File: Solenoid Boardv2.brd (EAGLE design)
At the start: 76.2 x 31.8 mm, 52 parts, among them Y2 ECS-80-S-4X

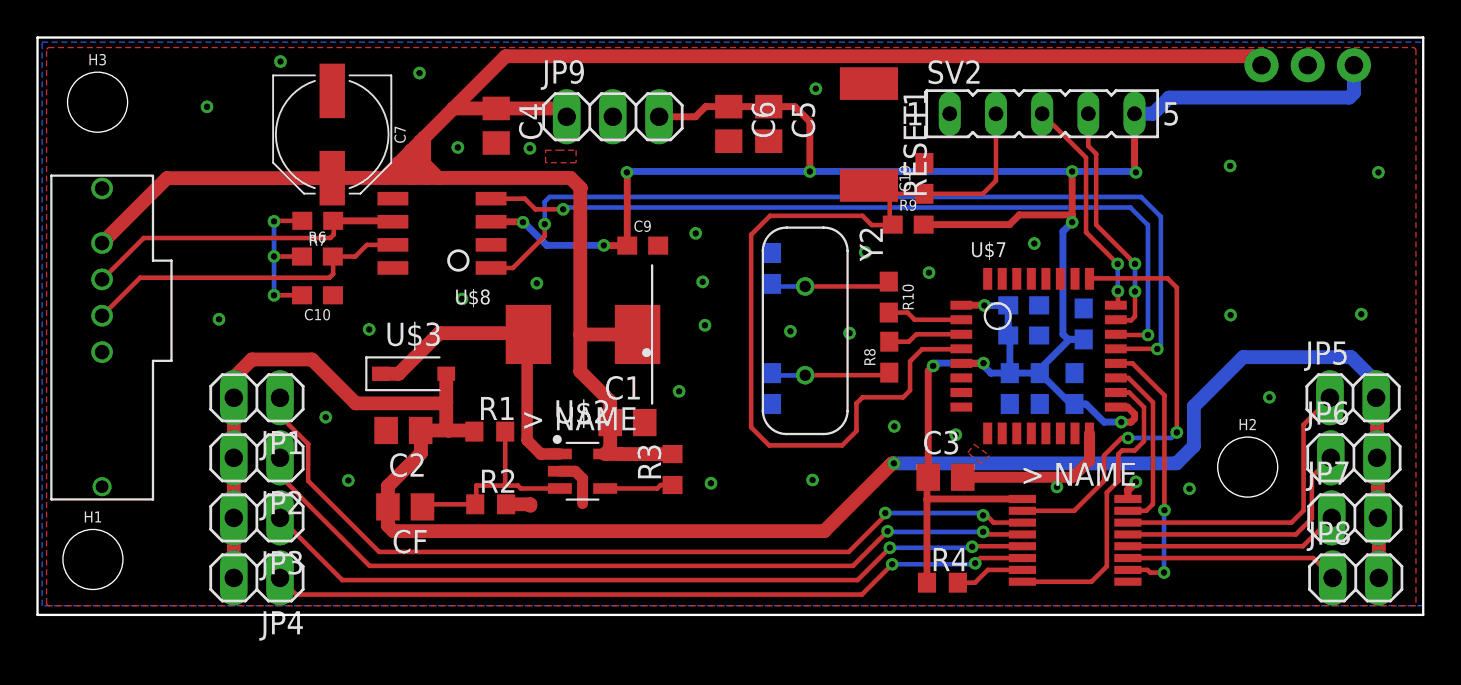
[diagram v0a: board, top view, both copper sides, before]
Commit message: fixed a weird trace, moved a standoff hole a little so that it didnt overlap with a trace
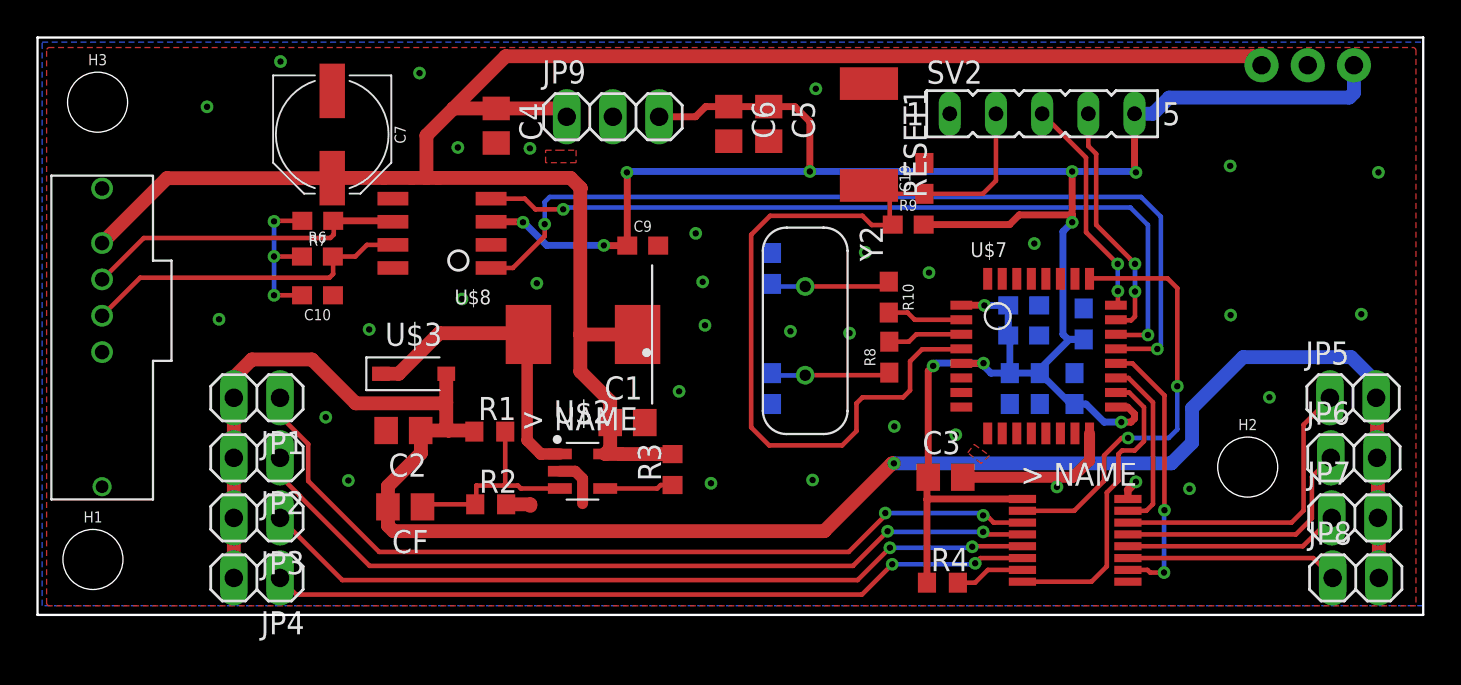
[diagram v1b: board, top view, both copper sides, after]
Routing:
- net +12V: track 115.5 -> 107.0 mm
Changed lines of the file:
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@@
 <wire x1="28.642" y1="27.85" x2="25.224" y2="27.85" width="0.762" layer="1"/>
 <wire x1="25.224" y1="27.85" x2="22.8716" y2="27.85" width="0.762" layer="1"/>
-<wire x1="22.8716" y1="27.85" x2="21.2598" y2="26.2382" width="0.762" layer="1"/>
-<wire x1="21.2598" y1="26.2382" x2="21.0566" y2="26.035" width="0.762" layer="1"/>
-<wire x1="21.0566" y1="26.035" x2="20.5486" y2="25.527" width="0.762" layer="1"/>
-<wire x1="20.5486" y1="25.527" x2="19.8628" y2="24.8412" width="0.762" layer="1"/>
-<wire x1="19.8628" y1="24.8412" x2="19.05" y2="24.0284" width="0.762" layer="1"/>
 <wire x1="19.05" y1="24.0284" x2="16.2176" y2="24.0284" width="0.762" layer="1"/>
 <wire x1="16.2176" y1="24.0284" x2="16.2052" y2="24.016" width="0.762" layer="1"/>
@@
 <wire x1="67.31" y1="30.226" x2="66.8147" y2="30.7213" width="0.762" layer="1"/>
 <wire x1="66.8147" y1="30.7213" x2="25.7429" y2="30.7213" width="0.762" layer="1"/>
-<wire x1="20.574" y1="24.0284" x2="19.8628" y2="24.7396" width="0.762" layer="1"/>
-<wire x1="19.8628" y1="24.7396" x2="19.8628" y2="24.8412" width="0.762" layer="1"/>
-<wire x1="20.5486" y1="25.527" x2="20.5486" y2="24.8666" width="0.762" layer="1"/>
-<wire x1="20.5486" y1="24.8666" x2="21.3868" y2="24.0284" width="0.762" layer="1"/>
-<wire x1="20.5486" y1="25.527" x2="21.0566" y2="25.019" width="0.762" layer="1"/>
-<wire x1="21.2598" y1="24.8158" x2="22.0472" y2="24.0284" width="0.762" layer="1"/>
-<wire x1="21.0566" y1="26.035" x2="21.0566" y2="25.019" width="0.762" layer="1"/>
-<wire x1="21.0566" y1="25.019" x2="21.2598" y2="24.8158" width="0.762" layer="1"/>
-<wire x1="21.2598" y1="26.2382" x2="21.2598" y2="24.8158" width="0.762" layer="1"/>
 <wire x1="29.8464" y1="23.4456" x2="29.8464" y2="15.4178" width="0.762" layer="1"/>
 <wire x1="31.2163" y1="8.85" x2="32.044" y2="8.85" width="0.762" layer="1"/>
@@
 <wire x1="31.492" y1="9.1257" x2="31.2163" y2="8.85" width="0.762" layer="1"/>
 <wire x1="31.492" y1="11.7452" x2="31.492" y2="10.5768" width="0.762" layer="1"/>
+<wire x1="22.8716" y1="27.85" x2="21.3868" y2="26.3652" width="0.762" layer="1"/>
+<wire x1="21.3868" y1="26.3652" x2="21.3868" y2="24.0284" width="0.762" layer="1"/>
 </signal>
 <signal name="+24V">
@@
 <wire x1="47.0916" y1="8.3312" x2="46.99" y2="8.3312" width="0.762" layer="1"/>
 <wire x1="46.99" y1="8.3312" x2="43.2646" y2="4.6058" width="0.762" layer="1"/>
-<wire x1="62.63363125" y1="8.334" x2="47.0944" y2="8.334" width="0.762" layer="16"/>
+<wire x1="62.35423125" y1="8.334" x2="47.0944" y2="8.334" width="0.762" layer="16"/>
 <wire x1="47.0944" y1="8.334" x2="47.0916" y2="8.3312" width="0.762" layer="16"/>
-<wire x1="63.5889125" y1="9.28928125" x2="62.63363125" y2="8.334" width="0.762" layer="16"/>
-<wire x1="63.5889125" y1="9.28928125" x2="63.5889125" y2="11.4681125" width="0.762" layer="16"/>
+<wire x1="63.4873125" y1="9.46708125" x2="62.35423125" y2="8.334" width="0.762" layer="16"/>
+<wire x1="63.4873125" y1="9.46708125" x2="63.4873125" y2="11.3665125" width="0.762" layer="16"/>
 <wire x1="72.2376" y1="14.1732" x2="66.294" y2="14.1732" width="0.762" layer="16"/>
 <wire x1="72.2376" y1="14.1732" x2="73.61" y2="12.8008" width="0.762" layer="16"/>
 <wire x1="73.61" y1="12.8008" x2="73.61" y2="11.938" width="0.762" layer="16"/>
-<wire x1="63.5889125" y1="11.4681125" x2="66.294" y2="14.1732" width="0.762" layer="16"/>
+<wire x1="63.4873125" y1="11.3665125" x2="66.294" y2="14.1732" width="0.762" layer="16"/>
 <wire x1="10.795" y1="2.032" x2="10.795" y2="5.334" width="0.762" layer="1"/>
 <wire x1="10.795" y1="5.334" x2="10.795" y2="8.636" width="0.762" layer="1"/>
@@
 <wire x1="58.6486" y1="8.763" x2="58.6486" y2="7.366" width="0.254" layer="1"/>
 <via x="59.9694" y="9.7282" extent="1-16" drill="0.35"/>
-<wire x1="62.6519125" y1="10.033" x2="62.3471125" y2="9.7282" width="0.254" layer="16"/>
-<wire x1="62.3471125" y1="9.7282" x2="59.9694" y2="9.7282" width="0.254" layer="16"/>
-<via x="62.6519125" y="10.033" extent="1-16" drill="0.35"/>
+<via x="62.6773125" y="12.573" extent="1-16" drill="0.35"/>
 <wire x1="57.0076" y1="5.725" x2="58.6486" y2="7.366" width="0.254" layer="1"/>
-<wire x1="62.6519125" y1="17.9930875" x2="62.6519125" y2="10.033" width="0.254" layer="1"/>
+<wire x1="62.6773125" y1="17.9676875" x2="62.6773125" y2="12.573" width="0.254" layer="1"/>
 <wire x1="62.1396" y1="18.5054" x2="57.8754" y2="18.5054" width="0.254" layer="1"/>
 <wire x1="57.8754" y1="18.5054" x2="57.85" y2="18.48" width="0.254" layer="1"/>
-<wire x1="62.6519125" y1="17.9930875" x2="62.1396" y2="18.5054" width="0.254" layer="1"/>
+<wire x1="62.6773125" y1="17.9676875" x2="62.1396" y2="18.5054" width="0.254" layer="1"/>
 <wire x1="54.16" y1="5.725" x2="57.0076" y2="5.725" width="0.254" layer="1"/>
+<wire x1="59.9694" y1="9.7282" x2="62.2046" y2="9.7282" width="0.254" layer="16"/>
+<wire x1="62.6773125" y1="10.2009125" x2="62.6773125" y2="12.573" width="0.254" layer="16"/>
+<wire x1="62.2046" y1="9.7282" x2="62.6773125" y2="10.2009125" width="0.254" layer="16"/>
 </signal>
 <signal name="G">
